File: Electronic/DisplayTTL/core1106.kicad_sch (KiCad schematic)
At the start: 1 part, among them U4 Core1106

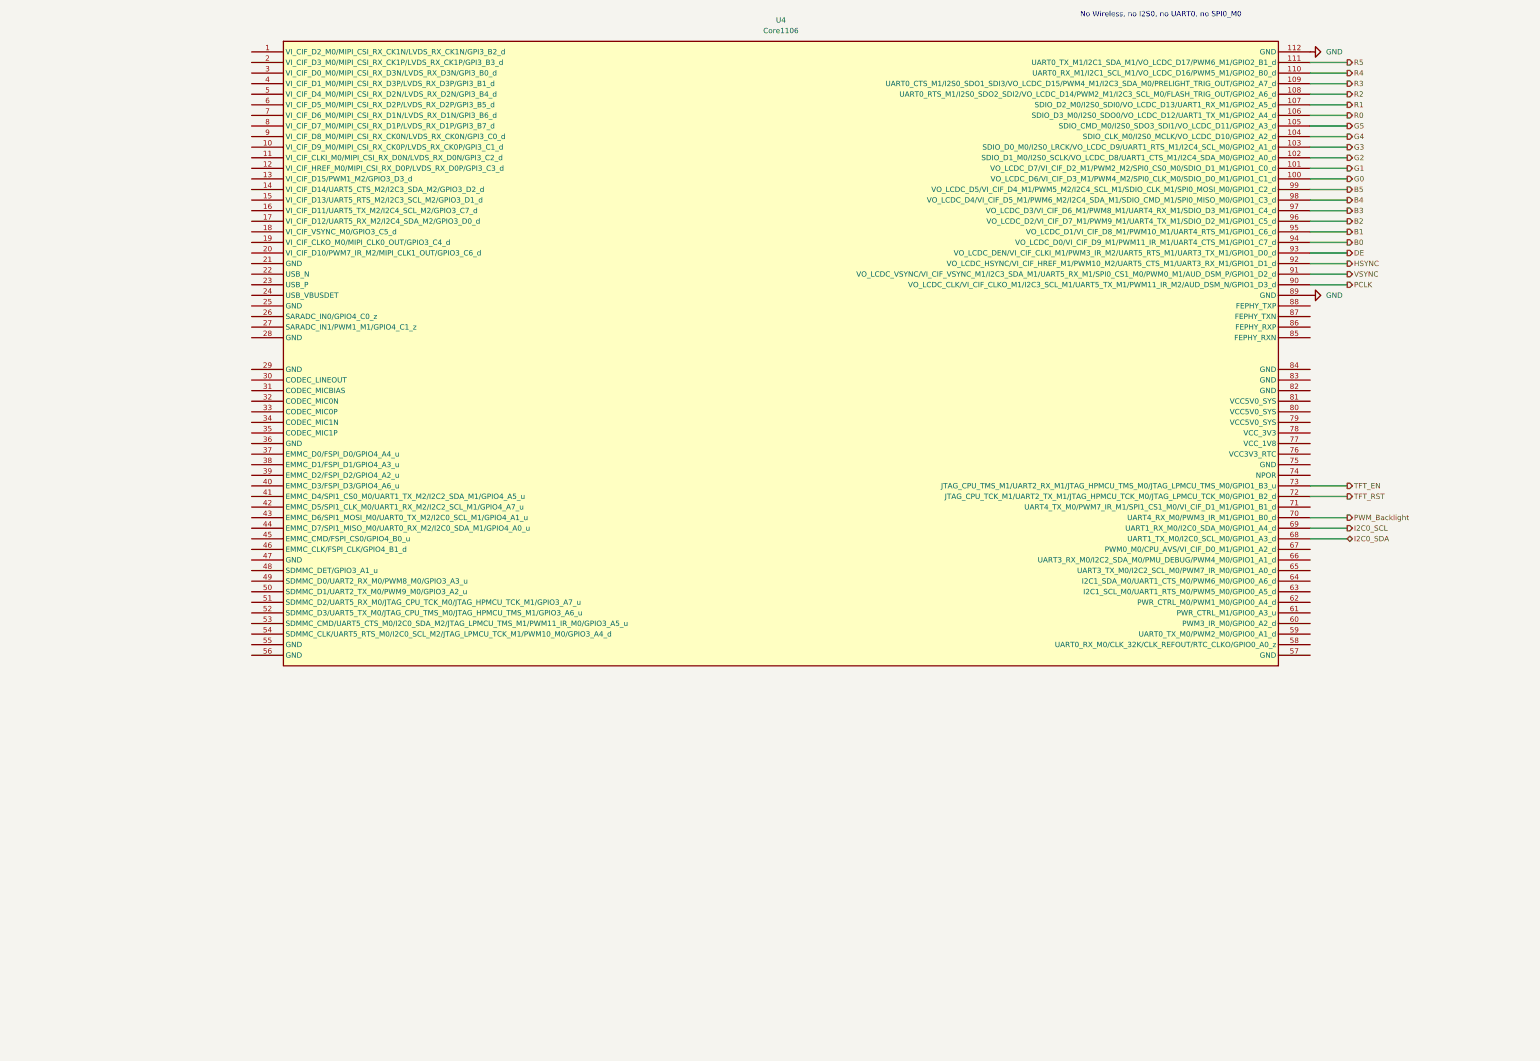
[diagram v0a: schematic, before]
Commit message: Add RV1106 RGB666 pinout doc: bus mapping, pin allocation, GPIO recovery plan
Schematic:
- Wire most of the gpios,
- Button for boot / reset
- DIsplay schematic done
- Wip I2S codec wiring on ESP32-P4 side
- Single Pair Ethernet T1S
- I2C ADC with 4 input
- Core1106 / ESP32-P4 wiring mostly done

WIP PCB layout / schematic.

Docs:
- Add Pico Pi schematic (use the Core1106 module)
- Add Makerworld url for stick and stick position
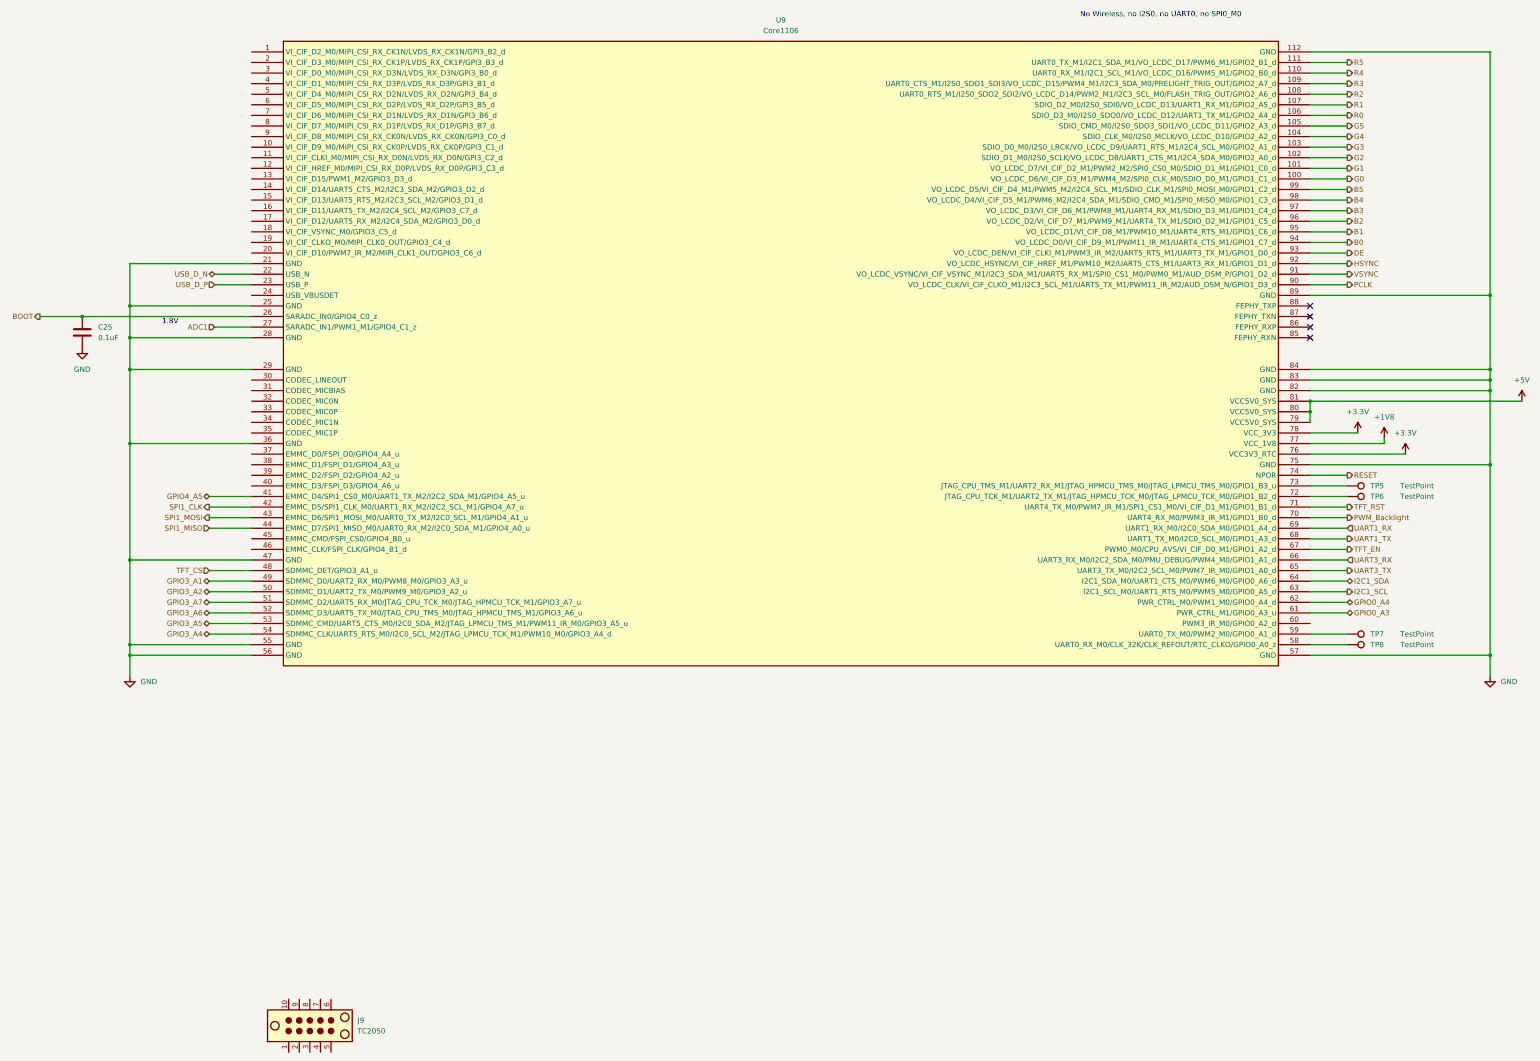
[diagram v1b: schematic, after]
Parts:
- added C25: 0.1uF, Capacitor_SMD:C_0402_1005Metric, symbol Device:C
- added J9: TC2050, Connector:Tag-Connect_TC2050-IDC-NL_2x05_P1.27mm_Vertical, symbol Connector:TC2050
- added TP5, TP6, TP7, TP8: TestPoint, symbol Connector:TestPoint
- renumbered U4 to U9
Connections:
- net GND: now also U9.21 (GND), U9.25 (GND), U9.28 (GND), U9.29 (GND), U9.36 (GND), U9.47 (GND), U9.55 (GND), U9.56 (GND), U9.57 (GND), U9.75 (GND), U9.82 (GND), U9.83 (GND), U9.84 (GND), C25.2
- net TFT_EN: now also U9.67 (PWM0_M0/CPU_AVS/VI_CIF_D0_M1/GPIO1_A2_d); no longer U9.73 (JTAG_CPU_TMS_M1/UART2_RX_M1/JTAG_HPMCU_TMS_M0/JTAG_LPMCU_TMS_M0/GPIO1_B3_u)
- net TFT_RST: now also U9.71 (UART4_TX_M0/PWM7_IR_M1/SPI1_CS1_M0/VI_CIF_D1_M1/GPIO1_B1_d); no longer U9.72 (JTAG_CPU_TCK_M1/UART2_TX_M1/JTAG_HPMCU_TCK_M0/JTAG_LPMCU_TCK_M0/GPIO1_B2_d)
- net USB_D_N: now reaches U9.22 (USB_N)
- net USB_D_P: now reaches U9.23 (USB_P)
- net BOOT: now reaches U9.26 (SARADC_IN0/GPIO4_C0_z)
- net BOOT: now also C25.1
- net ADC1: now reaches U9.27 (SARADC_IN1/PWM1_M1/GPIO4_C1_z)
- net GPIO4_A5: now reaches U9.41 (EMMC_D4/SPI1_CS0_M0/UART1_TX_M2/I2C2_SDA_M1/GPIO4_A5_u)
- net SPI1_CLK: now reaches U9.42 (EMMC_D5/SPI1_CLK_M0/UART1_RX_M2/I2C2_SCL_M1/GPIO4_A7_u)
- net SPI1_MOSI: now reaches U9.43 (EMMC_D6/SPI1_MOSI_M0/UART0_TX_M2/I2C0_SCL_M1/GPIO4_A1_u)
- net SPI1_MISO: now reaches U9.44 (EMMC_D7/SPI1_MISO_M0/UART0_RX_M2/I2C0_SDA_M1/GPIO4_A0_u)
- net TFT_CS: now reaches U9.48 (SDMMC_DET/GPIO3_A1_u)
- net GPIO3_A1: now reaches U9.49 (SDMMC_D0/UART2_RX_M0/PWM8_M0/GPIO3_A3_u)
- net GPIO3_A2: now reaches U9.50 (SDMMC_D1/UART2_TX_M0/PWM9_M0/GPIO3_A2_u)
- net GPIO3_A7: now reaches U9.51 (SDMMC_D2/UART5_RX_M0/JTAG_CPU_TCK_M0/JTAG_HPMCU_TCK_M1/GPIO3_A7_u)
- net GPIO3_A6: now reaches U9.52 (SDMMC_D3/UART5_TX_M0/JTAG_CPU_TMS_M0/JTAG_HPMCU_TMS_M1/GPIO3_A6_u)
- net GPIO3_A5: now reaches U9.53 (SDMMC_CMD/UART5_CTS_M0/I2C0_SDA_M2/JTAG_LPMCU_TMS_M1/PWM11_IR_M0/GPIO3_A5_u)
- net GPIO3_A4: now reaches U9.54 (SDMMC_CLK/UART5_RTS_M0/I2C0_SCL_M2/JTAG_LPMCU_TCK_M1/PWM10_M0/GPIO3_A4_d)
- net at U9.58 (UART0_RX_M0/CLK_32K/CLK_REFOUT/RTC_CLKO/GPIO0_A0_z): now also TP8.1
- net at U9.59 (UART0_TX_M0/PWM2_M0/GPIO0_A1_d): now also TP7.1
- net GPIO0_A3: now reaches U9.61 (PWR_CTRL_M1/GPIO0_A3_u)
- net GPIO0_A4: now reaches U9.62 (PWR_CTRL_M0/PWM1_M0/GPIO0_A4_d)
- net I2C1_SCL: now reaches U9.63 (I2C1_SCL_M0/UART1_RTS_M0/PWM5_M0/GPIO0_A5_d)
- net I2C1_SDA: now reaches U9.64 (I2C1_SDA_M0/UART1_CTS_M0/PWM6_M0/GPIO0_A6_d)
- net UART3_TX: now reaches U9.65 (UART3_TX_M0/I2C2_SCL_M0/PWM7_IR_M0/GPIO1_A0_d)
- net UART3_RX: now reaches U9.66 (UART3_RX_M0/I2C2_SDA_M0/PMU_DEBUG/PWM4_M0/GPIO1_A1_d)
- net RESET: now reaches U9.74 (NPOR)
- net +3.3V: now reaches U9.76 (VCC3V3_RTC)
- net +3.3V: now also U9.78 (VCC_3V3)
- net +1V8: now reaches U9.77 (VCC_1V8)
- net +5V: now reaches U9.79 (VCC5V0_SYS)
- net +5V: now also U9.80 (VCC5V0_SYS), U9.81 (VCC5V0_SYS)
- net I2C0_SCL renamed UART1_RX
- net I2C0_SDA renamed UART1_TX
- new net: TP6.1, U9.72 (JTAG_CPU_TCK_M1/UART2_TX_M1/JTAG_HPMCU_TCK_M0/JTAG_LPMCU_TCK_M0/GPIO1_B2_d)
- new net: TP5.1, U9.73 (JTAG_CPU_TMS_M1/UART2_RX_M1/JTAG_HPMCU_TMS_M0/JTAG_LPMCU_TMS_M0/GPIO1_B3_u)
- no-connect marks 0 -> 4
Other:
- note added: "1.8V"
